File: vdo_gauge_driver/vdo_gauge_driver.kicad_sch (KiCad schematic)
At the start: 15 parts, among them J1 ECU input, J2 Gauge S, J3 Gauge V-, J4 Gauge V+, SW1 SW_SPDT, U1 L7805, U3 MCP6002-xP, U4 ATtiny85-20P

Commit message: Update the cad drawings
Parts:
- removed J1: ECU input, symbol Connector:Screw_Terminal_01x01
- removed J2: Gauge S, symbol Connector:Screw_Terminal_01x01
- removed J3: Gauge V-, symbol Connector:Screw_Terminal_01x01
- removed J4: Gauge V+, symbol Connector:Screw_Terminal_01x01
- added J1: 12V and GND, Connector_JST:JST_XH_B2B-XH-A_1x02_P2.50mm_Vertical, symbol Connector:Conn_01x02_Socket
- added J2: 12V / Signal / GND, Connector_JST:JST_XH_B3B-XH-A_1x03_P2.50mm_Vertical, symbol Connector:Conn_01x03_Socket
- added J3: ECU Input, Connector_JST:JST_XH_B1B-XH-AM_1x01_P2.50mm_Vertical, symbol Connector:Conn_01x01_Socket
- C1, C2: footprint (none) -> Capacitor_THT:C_Disc_D6.0mm_W2.5mm_P5.00mm
- C3: footprint (none) -> Capacitor_THT:C_Radial_D5.0mm_H7.0mm_P2.00mm
- R1, R2, R3: footprint (none) -> Resistor_THT:R_Axial_DIN0309_L9.0mm_D3.2mm_P12.70mm_Horizontal
- RV1: footprint (none) -> Potentiometer_THT:Potentiometer_Bourns_3386P_Vertical
- SW1: footprint (none) -> Button_Switch_THT:SW_Slide-03_Wuerth-WS-SLTV_10x2.5x6.4_P2.54mm
- U1: footprint (none) -> Package_TO_SOT_THT:TO-220-3_Horizontal_TabDown
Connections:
- net GND: now also J1.2 (Pin_2), J2.3 (Pin_3)
- net 5V: now reaches C2.1, RV1.1, U1.3 (OUT), U3.8 (V+), U4.8 (VCC)
- net op-amped signal: now reaches U3.1, U3.2 (-), U4.2 (XTAL1/PB3)
- net Input: now reaches U3.3 (+)
- net Input: now also SW1.1 (A); no longer SW1.2 (B)
- net 0-10V: now reaches R3.1, U3.7
- net 0-10V: now also J2.2 (Pin_2)
- net ECU Input: now reaches SW1.3 (C)
- net ECU Input: now also J3.1 (Pin_1); no longer RV1.2
- net +12V renamed 12V
- net 12V: now also J1.1 (Pin_1), J2.1 (Pin_1)
- new net Testing 0-5V: RV1.2, SW1.2 (B)
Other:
- moved on the sheet: C3, R1, R2, R3, SW1, U3B

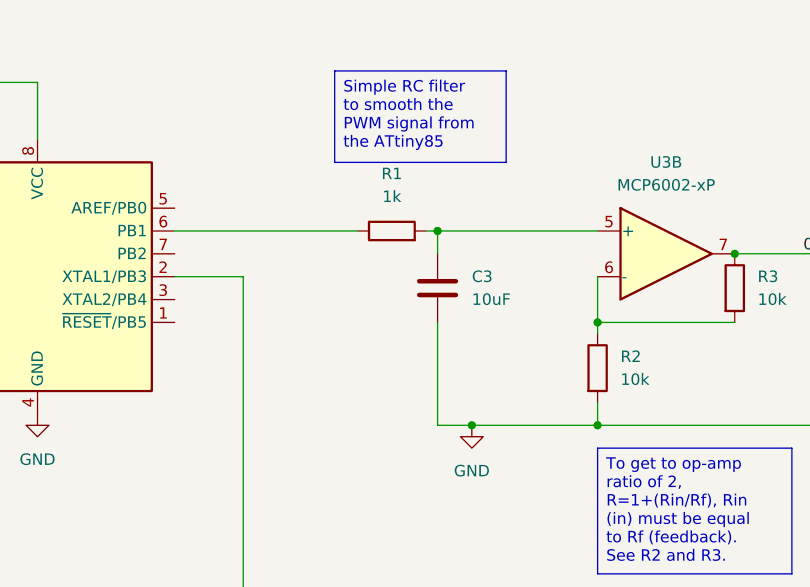
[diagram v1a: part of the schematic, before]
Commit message: Adding datasheets, working on README, python generated graph and values
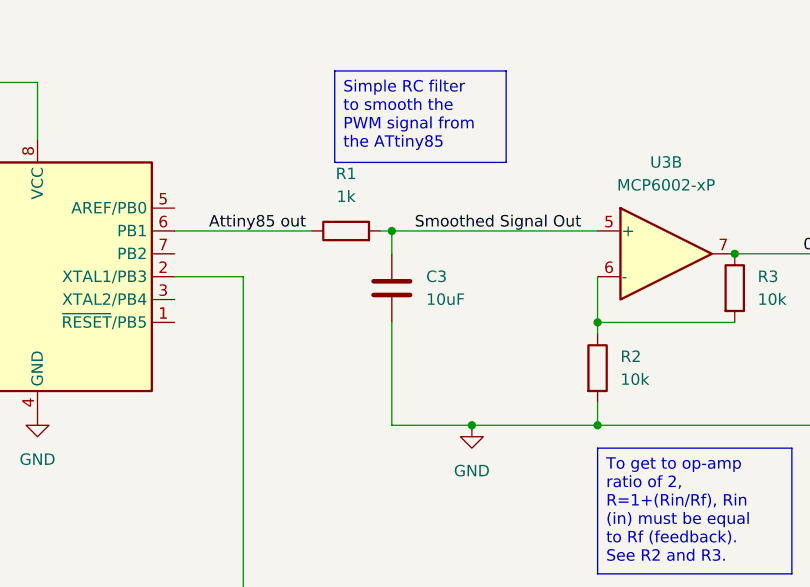
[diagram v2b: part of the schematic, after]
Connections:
- net Attiny85 out: now reaches R1.1, U4.6 (PB1)
- net Smoothed Signal Out: now reaches C3.1, R1.2, U3.5 (+)
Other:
- title: Porsche 996 VDO Vision Oil Tempearature Gauge Driver -> VDO Vision Oil Tempearature Gauge Driver
- moved on the sheet: C3, R1
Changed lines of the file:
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@@
 	(paper "A4")
 	(title_block
-		(title "Porsche 996 VDO Vision Oil Tempearature Gauge Driver")
+		(title "VDO Vision Oil Tempearature Gauge Driver")
 		(date "2025-05-04")
 		(rev "0.1")
@@
 	)
 	(junction
+		(at 200.66 82.55)
+		(diameter 0)
+		(color 0 0 0 0)
+	)
+	(junction
 		(at 88.9 96.52)
 		(diameter 0)
@@
 	)
 	(junction
-		(at 205.74 82.55)
-		(diameter 0)
-		(color 0 0 0 0)
-	)
-	(junction
 		(at 36.83 66.04)
 		(diameter 0)
@@
 	(wire
 		(pts
-			(xy 176.53 82.55) (xy 196.85 82.55)
+			(xy 176.53 82.55) (xy 191.77 82.55)
 		)
 		(stroke
@@
 	(wire
 		(pts
-			(xy 205.74 82.55) (xy 223.52 82.55)
-		)
-		(stroke
-			(width 0)
-			(type default)
-		)
-	)
-	(wire
-		(pts
 			(xy 254 87.63) (xy 254 104.14)
 		)
@@
 	(wire
 		(pts
-			(xy 204.47 82.55) (xy 205.74 82.55)
-		)
-		(stroke
-			(width 0)
-			(type default)
-		)
-	)
-	(wire
-		(pts
-			(xy 209.55 104.14) (xy 205.74 104.14)
+			(xy 199.39 82.55) (xy 200.66 82.55)
+		)
+		(stroke
+			(width 0)
+			(type default)
+		)
+	)
+	(wire
+		(pts
+			(xy 209.55 104.14) (xy 200.66 104.14)
 		)
 		(stroke
@@
 	(wire
 		(pts
-			(xy 205.74 92.71) (xy 205.74 104.14)
+			(xy 200.66 92.71) (xy 200.66 104.14)
 		)
 		(stroke
@@
 	(wire
 		(pts
+			(xy 200.66 82.55) (xy 223.52 82.55)
+		)
+		(stroke
+			(width 0)
+			(type default)
+		)
+	)
+	(wire
+		(pts
 			(xy 119.38 88.9) (xy 119.38 107.95)
 		)
@@
 	(wire
 		(pts
-			(xy 205.74 85.09) (xy 205.74 82.55)
+			(xy 200.66 85.09) (xy 200.66 82.55)
 		)
 		(stroke
@@
 	(label "Testing 0-5V"
 		(at 104.14 107.95 0)
+		(effects
+			(font
+				(size 1.27 1.27)
+			)
+			(justify left bottom)
+		)
+	)
+	(label "Smoothed Signal Out"
+		(at 203.2 82.55 0)
+		(effects
+			(font
+				(size 1.27 1.27)
+			)
+			(justify left bottom)
+		)
+	)
+	(label "Attiny85 out"
+		(at 180.34 82.55 0)
 		(effects
 			(font
@@
 	(symbol
 		(lib_id "Device:C")
-		(at 205.74 88.9 0)
+		(at 200.66 88.9 0)
 		(unit 1)
 		(exclude_from_sim no)
@@
 		(fields_autoplaced yes)
 		(property "Reference" "C3"
-			(at 209.55 87.6299 0)
+			(at 204.47 87.6299 0)
 			(effects
 				(font
@@
 		)
 		(property "Value" "10uF"
-			(at 209.55 90.1699 0)
+			(at 204.47 90.1699 0)
 			(effects
 				(font
@@
 		)
 		(property "Footprint" "Capacitor_THT:C_Radial_D5.0mm_H7.0mm_P2.00mm"
-			(at 206.7052 92.71 0)
+			(at 201.6252 92.71 0)
 			(effects
 				(font
@@
 		)
 		(property "Datasheet" "~"
-			(at 205.74 88.9 0)
+			(at 200.66 88.9 0)
 			(effects
 				(font
@@
 		)
 		(property "Description" "Unpolarized capacitor"
-			(at 205.74 88.9 0)
+			(at 200.66 88.9 0)
 			(effects
 				(font
@@
 	(symbol
 		(lib_id "Device:R")
-		(at 200.66 82.55 90)
+		(at 195.58 82.55 90)
 		(unit 1)
 		(exclude_from_sim no)
@@
 		(dnp no)
 		(property "Reference" "R1"
-			(at 200.66 76.2 90)
+			(at 195.58 76.2 90)
 			(effects
 				(font
@@
 		)
 		(property "Value" "1k"
-			(at 200.66 78.74 90)
+			(at 195.58 78.74 90)
 			(effects
 				(font
@@
 		)
 		(property "Footprint" "Resistor_THT:R_Axial_DIN0309_L9.0mm_D3.2mm_P12.70mm_Horizontal"
-			(at 200.66 84.328 90)
+			(at 195.58 84.328 90)
 			(effects
 				(font
@@
 		)
 		(property "Datasheet" "~"
-			(at 200.66 82.55 0)
+			(at 195.58 82.55 0)
 			(effects
 				(font
@@
 		)
 		(property "Description" "Resistor"
-			(at 200.66 82.55 0)
-			(effects
-				(font
+			(at 195.58 82.55 0)
+			(effects
+				(font

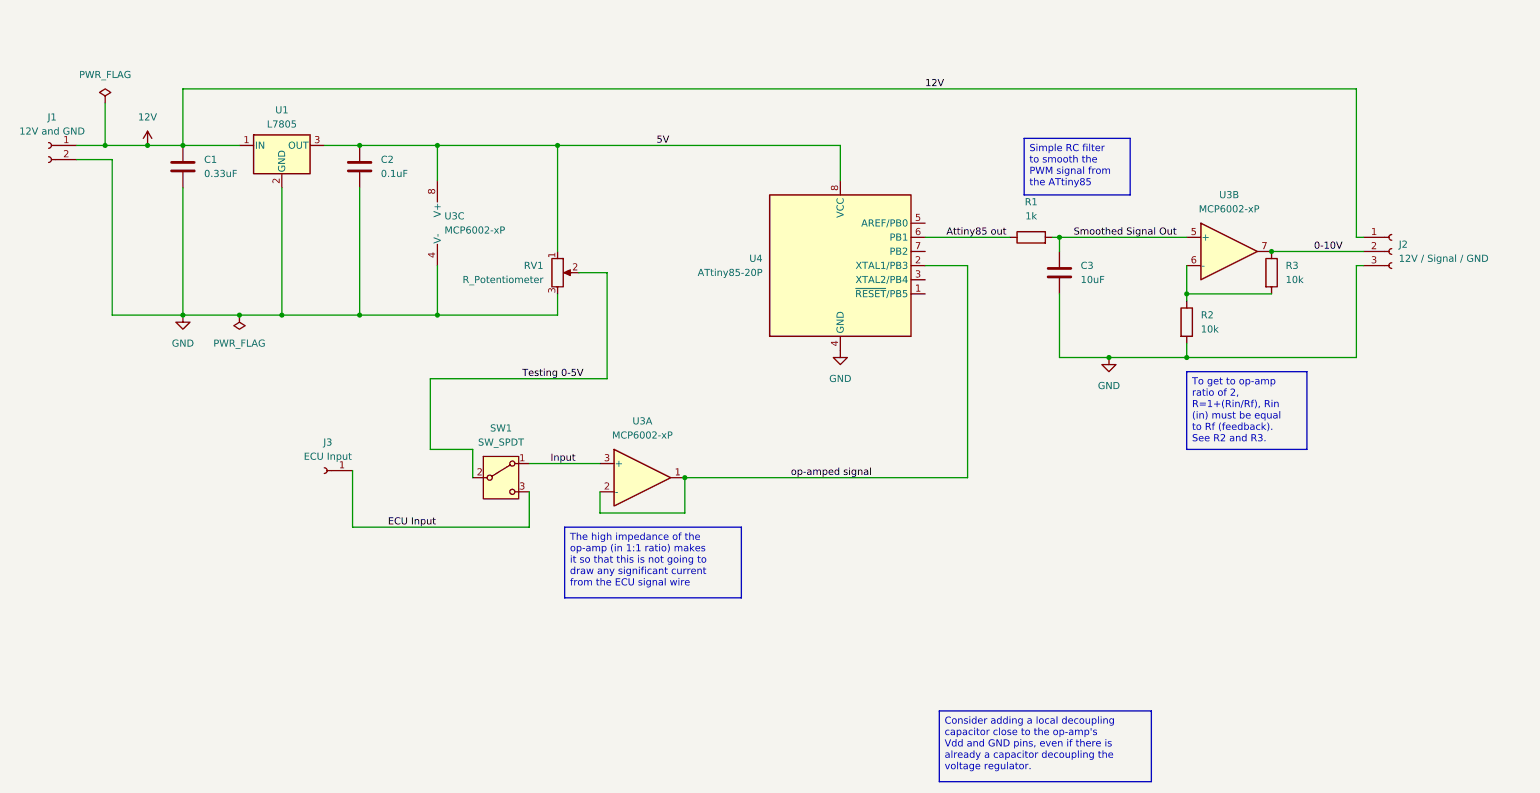
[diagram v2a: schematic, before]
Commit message: Change to use the MOSFET
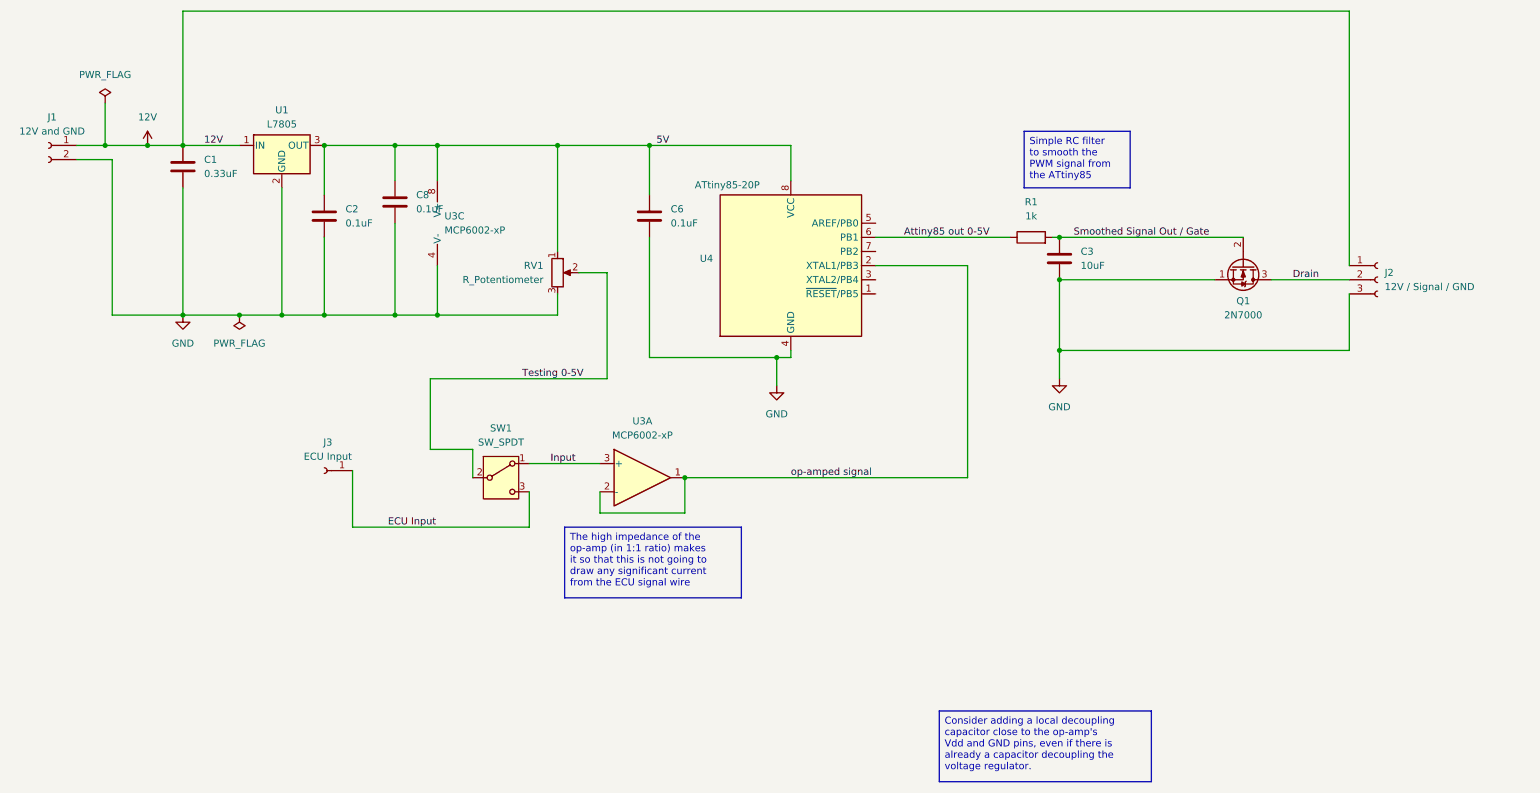
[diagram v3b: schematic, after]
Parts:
- removed R2, R3: 10k, Resistor_THT:R_Axial_DIN0309_L9.0mm_D3.2mm_P12.70mm_Horizontal, symbol Device:R
- removed unit 2 of U3
- added C6, C8: 0.1uF, Capacitor_THT:C_Disc_D6.0mm_W2.5mm_P5.00mm, symbol Device:C
- added Q1: 2N7000, Package_TO_SOT_THT:TO-92_Inline, symbol Transistor_FET:2N7000
- U3: footprint (none) -> Package_DIP:DIP-8_W7.62mm
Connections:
- net 5V: now also C6.1, C8.1
- net GND: now also C6.2, C8.2, Q1.1 (S)
- net 0-10V renamed Drain
- net Drain: now also Q1.3 (D)
- net Attiny85 out renamed Attiny85 out 0-5V
- net Smoothed Signal Out renamed Smoothed Signal Out / Gate
- net Smoothed Signal Out / Gate: now also Q1.2 (G)
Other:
- moved on the sheet: C2, C3, J2, U4

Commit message: Working, but unstable
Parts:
- removed RV1: R_Potentiometer, Potentiometer_THT:Potentiometer_Bourns_3386P_Vertical, symbol Device:R_Potentiometer
- removed SW1: SW_SPDT, Button_Switch_THT:SW_Slide-03_Wuerth-WS-SLTV_10x2.5x6.4_P2.54mm, symbol Switch:SW_SPDT
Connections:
- net Input is gone; now on net ECU Input: U3.3 (+)
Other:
- moved on the sheet: J3, U3C

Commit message: Updated schematics
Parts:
- added R2: 22R, symbol Device:R
- added U2: MCP6002-xP, symbol Amplifier_Operational:MCP6002-xP
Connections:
- net GND: now also R2.2; no longer Q1.1 (S)
- net Smoothed Signal Out / Gate: now also U2.5 (+); no longer Q1.2 (G)
- new net: Q1.1 (S), R2.1, U2.6 (-)
- new net: Q1.2 (G), U2.7
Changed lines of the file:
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@@
 	(text_box "Simple RC filter to smooth the PWM signal from the ATtiny85"
 		(exclude_from_sim no)
-		(at 194.31 63.5 0)
+		(at 179.07 62.23 0)
 		(size 19.05 10.16)
 		(margins 0.9525 0.9525 0.9525 0.9525)
@@
 	)
 	(junction
-		(at 200.66 90.17)
-		(diameter 0)
-		(color 0 0 0 0)
-	)
-	(junction
 		(at 29.21 66.04)
 		(diameter 0)
@@
 	)
 	(junction
+		(at 200.66 82.55)
+		(diameter 0)
+		(color 0 0 0 0)
+	)
+	(junction
 		(at 81.28 96.52)
 		(diameter 0)
@@
 	)
 	(junction
+		(at 228.6 73.66)
+		(diameter 0)
+		(color 0 0 0 0)
+	)
+	(junction
 		(at 200.66 102.87)
 		(diameter 0)
@@
 	)
 	(junction
-		(at 200.66 82.55)
-		(diameter 0)
-		(color 0 0 0 0)
-	)
-	(junction
 		(at 43.18 66.04)
 		(diameter 0)
@@
 	)
 	(junction
+		(at 218.44 102.87)
+		(diameter 0)
+		(color 0 0 0 0)
+	)
+	(junction
 		(at 68.58 96.52)
 		(diameter 0)
@@
 	(wire
 		(pts
+			(xy 245.11 82.55) (xy 233.68 82.55)
+		)
+		(stroke
+			(width 0)
+			(type default)
+		)
+	)
+	(wire
+		(pts
 			(xy 238.76 90.17) (xy 252.73 90.17)
 		)
@@
 	(wire
 		(pts
-			(xy 200.66 82.55) (xy 233.68 82.55)
-		)
-		(stroke
-			(width 0)
-			(type default)
-		)
-	)
-	(wire
-		(pts
 			(xy 60.96 96.52) (xy 68.58 96.52)
 		)
@@
 	(wire
 		(pts
+			(xy 218.44 83.82) (xy 218.44 102.87)
+		)
+		(stroke
+			(width 0)
+			(type default)
+		)
+	)
+	(wire
+		(pts
 			(xy 81.28 66.04) (xy 96.52 66.04)
 		)
@@
 	(wire
 		(pts
+			(xy 228.6 90.17) (xy 228.6 73.66)
+		)
+		(stroke
+			(width 0)
+			(type default)
+		)
+	)
+	(wire
+		(pts
 			(xy 127 104.14) (xy 149.86 104.14)
 		)
@@
 	(wire
 		(pts
+			(xy 200.66 82.55) (xy 200.66 68.58)
+		)
+		(stroke
+			(width 0)
+			(type default)
+		)
+	)
+	(wire
+		(pts
 			(xy 68.58 66.04) (xy 81.28 66.04)
 		)
@@
 	(wire
 		(pts
-			(xy 200.66 90.17) (xy 228.6 90.17)
-		)
-		(stroke
-			(width 0)
-			(type default)
-		)
-	)
-	(wire
-		(pts
 			(xy 152.4 104.14) (xy 149.86 104.14)
 		)
@@
 	(wire
 		(pts
-			(xy 252.73 102.87) (xy 200.66 102.87)
+			(xy 252.73 102.87) (xy 218.44 102.87)
+		)
+		(stroke
+			(width 0)
+			(type default)
+		)
+	)
+	(wire
+		(pts
+			(xy 218.44 102.87) (xy 200.66 102.87)
 		)
 		(stroke
@@
 	(wire
 		(pts
+			(xy 200.66 68.58) (xy 229.87 68.58)
+		)
+		(stroke
+			(width 0)
+			(type default)
+		)
+	)
+	(wire
+		(pts
 			(xy 53.34 96.52) (xy 60.96 96.52)
 		)
@@
 	(wire
 		(pts
+			(xy 228.6 73.66) (xy 229.87 73.66)
+		)
+		(stroke
+			(width 0)
+			(type default)
+		)
+	)
+	(wire
+		(pts
+			(xy 228.6 73.66) (xy 218.44 73.66)
+		)
+		(stroke
+			(width 0)
+			(type default)
+		)
+	)
+	(wire
+		(pts
 			(xy 252.73 87.63) (xy 252.73 41.91)
 		)
@@
 	(wire
 		(pts
+			(xy 218.44 73.66) (xy 218.44 76.2)
+		)
+		(stroke
+			(width 0)
+			(type default)
+		)
+	)
+	(wire
+		(pts
 			(xy 200.66 102.87) (xy 200.66 107.95)
 		)
@@
 		(pts
 			(xy 68.58 82.55) (xy 68.58 96.52)
+		)
+		(stroke
+			(width 0)
+			(type default)
+		)
+	)
+	(wire
+		(pts
+			(xy 245.11 71.12) (xy 245.11 82.55)
 		)
 		(stroke
@@
 	)
 	(label "Smoothed Signal Out {slash} Gate"
-		(at 203.2 82.55 0)
+		(at 200.66 68.58 0)
 		(effects
 			(font
@@
 			)
 			(justify left bottom)
+		)
+	)
+	(symbol
+		(lib_id "Device:R")
+		(at 218.44 80.01 0)
+		(unit 1)
+		(exclude_from_sim no)
+		(in_bom yes)
+		(on_board yes)
+		(dnp no)
+		(fields_autoplaced yes)
+		(property "Reference" "R2"
+			(at 220.98 78.7399 0)
+			(effects
+				(font
+					(size 1.27 1.27)
+				)
+				(justify left)
+			)
+		)
+		(property "Value" "22R"
+			(at 220.98 81.2799 0)
+			(effects
+				(font
+					(size 1.27 1.27)
+				)
+				(justify left)
+			)
+		)
+		(property "Footprint" ""
+			(at 216.662 80.01 90)
+			(effects
+				(font
+					(size 1.27 1.27)
+				)
+				(hide yes)
+			)
+		)
+		(property "Datasheet" "~"
+			(at 218.44 80.01 0)
+			(effects
+				(font
+					(size 1.27 1.27)
+				)
+				(hide yes)
+			)
+		)
+		(property "Description" "Resistor"
+			(at 218.44 80.01 0)
+			(effects
+				(font
+					(size 1.27 1.27)
+				)
+				(hide yes)
+			)
+		)
+		(pin "1"
+		)
+		(pin "2"
+		)
+		(instances
+			(project ""
+				(path "/5522c6c2-0190-4a1a-827d-62998a7dbe1c"
+					(reference "R2")
+					(unit 1)
+				)
+			)
 		)
 	)
@@
 				)
 			)
+		)
+	)
+	(symbol
+		(lib_id "Amplifier_Operational:MCP6002-xP")
+		(at 237.49 71.12 0)
+		(unit 2)
+		(exclude_from_sim no)
+		(in_bom yes)
+		(on_board yes)
+		(dnp no)
+		(fields_autoplaced yes)
+		(property "Reference" "U2"
+			(at 237.49 60.96 0)
+			(effects
+				(font
+					(size 1.27 1.27)
+				)
+			)
+		)
+		(property "Value" "MCP6002-xP"
+			(at 237.49 63.5 0)
+			(effects
+				(font
+					(size 1.27 1.27)
+				)
+			)
+		)
+		(property "Footprint" ""
+			(at 237.49 71.12 0)
+			(effects
+				(font
+					(size 1.27 1.27)
+				)
+				(hide yes)
+			)
+		)
+		(property "Datasheet" "http://ww1.microchip.com/downloads/en/DeviceDoc/21733j.pdf"
+			(at 237.49 71.12 0)
+			(effects
+				(font
+					(size 1.27 1.27)
+				)
+				(hide yes)
+			)
+		)
+		(property "Description" "1MHz, Low-Power Op Amp, DIP-8"
+			(at 237.49 71.12 0)
+			(effects
+				(font
+					(size 1.27 1.27)
+				)
+				(hide yes)
+			)
+		)
+		(pin "3"
+		)
+		(pin "2"
+		)
+		(pin "7"
+		)
+		(pin "1"
+		)
+		(pin "8"
+		)
+		(pin "4"
+		)
+		(pin "6"
+		)
+		(pin "5"
+		)
+		(instances
+			(project ""
+				(path "/5522c6c2-0190-4a1a-827d-62998a7dbe1c"
+					(reference "U2")
+					(unit 2)
+				)
+			)

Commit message: Major commit :)
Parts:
- Q1: value 2N7000 -> BS170
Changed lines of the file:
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@@
 	(title_block
 		(title "VDO Vision Oil Tempearature Gauge Driver")
-		(date "2025-05-04")
-		(rev "0.1")
+		(date "2025-05-24")
+		(rev "0.2")
 	)
 	(text_box "Simple RC filter to smooth the PWM signal from the ATtiny85"
@@
 		(at 179.07 62.23 0)
 		(size 19.05 10.16)
-		(margins 0.9525 0.9525 0.9525 0.9525)
-		(stroke
-			(width 0)
-			(type solid)
-		)
-		(fill
-			(type none)
-		)
-		(effects
-			(font
-				(size 1.27 1.27)
-			)
-			(justify left top)
-		)
-	)
-	(text_box "Consider adding a local decoupling capacitor close to the op-amp's Vdd and GND pins, even if there is already a capacitor decoupling the voltage regulator."
-		(exclude_from_sim no)
-		(at 179.07 167.64 0)
-		(size 38.1 12.7)
 		(margins 0.9525 0.9525 0.9525 0.9525)
 		(stroke
@@
 			)
 		)
-		(property "Value" "2N7000"
+		(property "Value" "BS170"
 			(at 233.68 96.52 90)
 			(effects
